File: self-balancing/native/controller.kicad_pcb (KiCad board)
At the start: 6 copper layers, 38 x 38 mm, 151 parts, among them J101 G, J102 5V, J103 T1, J104 R1, J105 G, J106 5V, J107 T2, J108 R2, J109 G, J110 5V, J111 T3, J112 R3, J113 G, J114 5V, J115 T4, J116 R4, J117 G, J118 3V3, J119 SCL, J120 SDA, J121 INT, J122 G, J123 G, J124 3V3, J125 SCK, J126 MISO, J127 MOSI, J128 CS, J129 G, J130 3V3, J131 CAN_RX, J132 CAN_TX, J133 G, J134 OUT1, J135 OUT2, J136 OUT3, J137 OUT4, J138 G, J139 OUT5, J140 OUT6, J141 OUT7, J142 OUT8, J143 G_LINK, J144 5V_LINK, J145 LINK_TX, J146 LINK_RX, J147 RUN, J148 M_OK, J149 G, J150 VTREF, J151 SWDIO, J152 SWCLK, J153 NRST, J154 BOOT, J155 G, J156 3V3, J157 ADC1, J158 ADC2, J159 ADC3, J160 RPM, J161 G, J162 3V3, J163 LED, J164 BUZ, J165 PC8, J166 PC9, J167 PD14, J2 TYPE-C-31-M-12, J3 MOTOR / 6-wire, J4 EXT SPI SENSOR, J5 GPS / UART4, Q1 2N7002, Q2 DMN2310UW-7, U1 STM32H743VIT6, U10 SN74LVC2G17DBVR, U11 W25N01GVZEIG / 128MiB, U12 TLV803EA29DBZR, U13 TPS2116DRLR, U2 TPS62162DSGR / 3.3V, U3 ICM-42688-P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

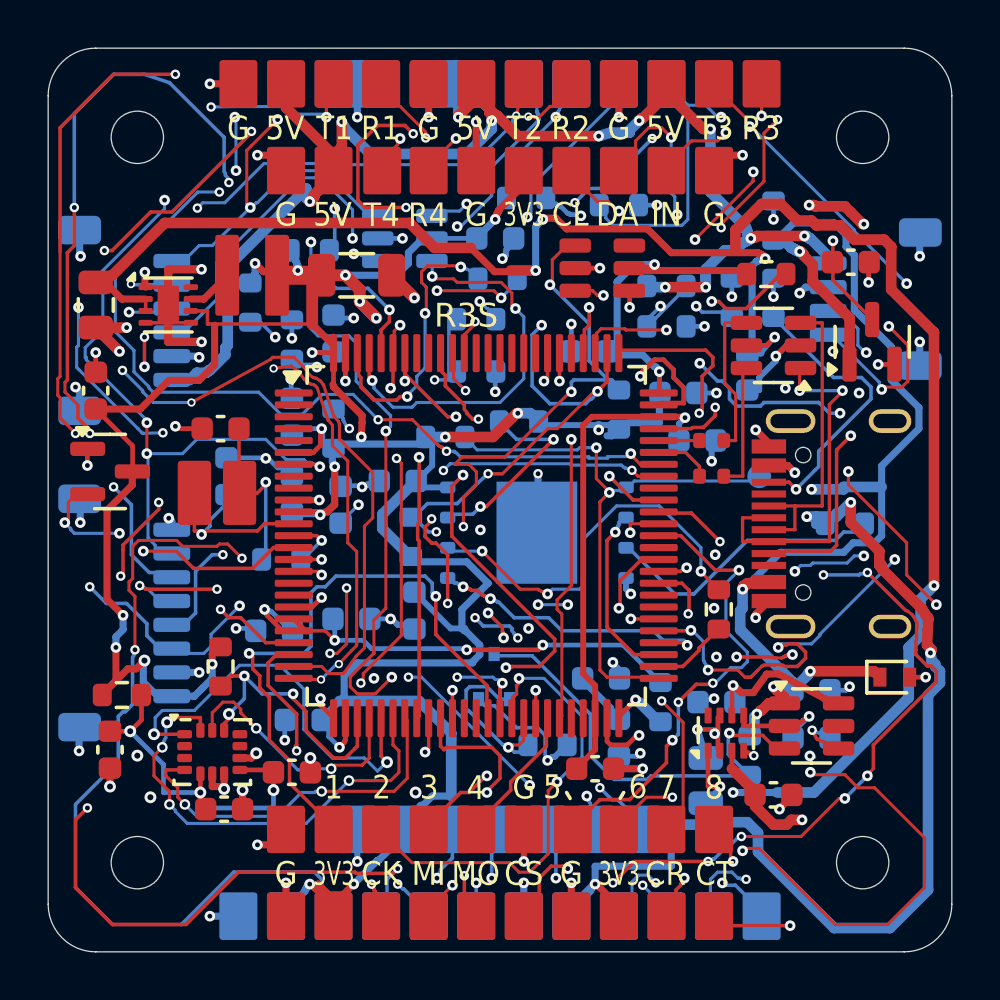
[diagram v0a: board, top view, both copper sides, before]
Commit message: Fix native USB routing and shallow via contacts
Native-only repair based on 491987e. Configured DRC/ERC/opens/parity pass. Keeps placement, BOM/CPL, 406 vias and 97 GND stitches. Manufacturing exports have not been regenerated; full validation evidence follows in this branch.
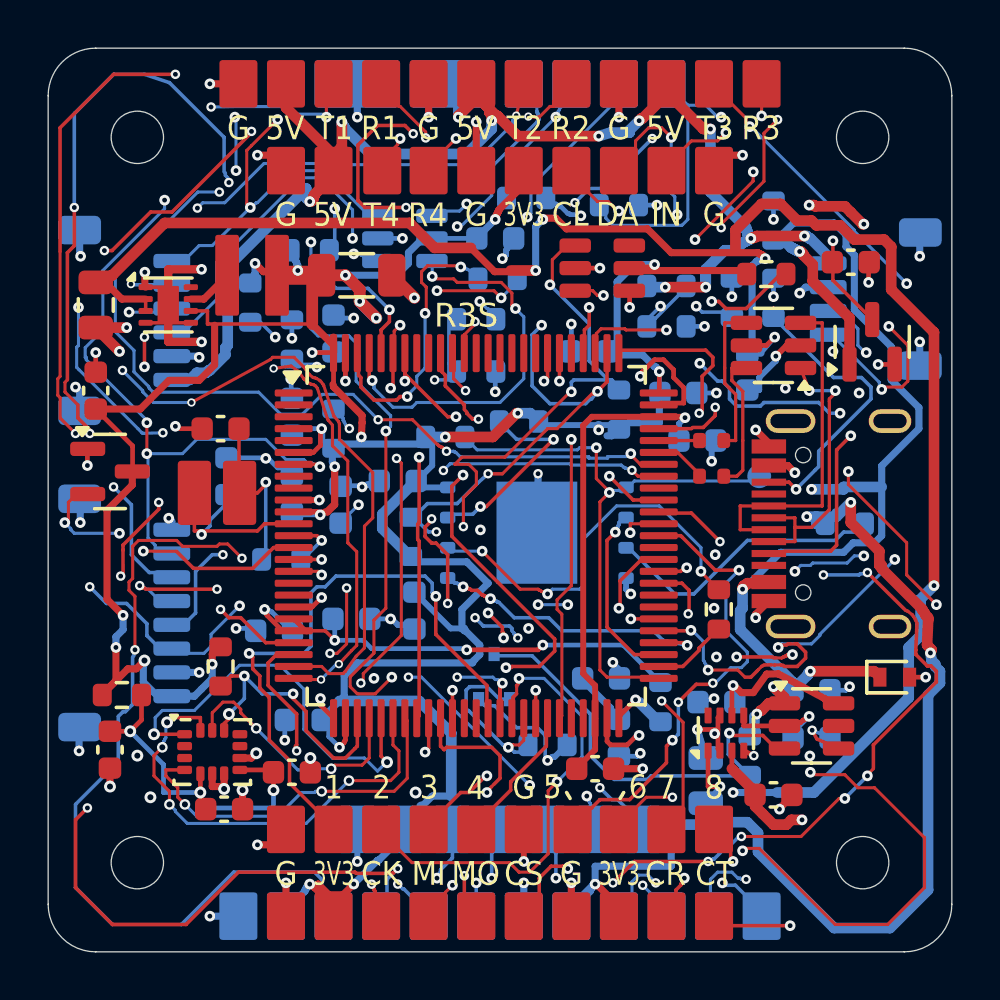
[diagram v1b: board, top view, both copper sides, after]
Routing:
- net /power/USB_CONN_N: track 15.1 -> 12.2 mm
- net /power/USB_CONN_P: track 13.0 -> 14.3 mm
- net /power/USB_ESD_N: track 5.50 -> 6.01 mm
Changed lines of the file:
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@@
 	)
 	(segment
-		(start 32.065878 29.8)
-		(end 32.029385 29.763507)
-		(width 0.2)
-		(layer "B.Cu")
-		(net "GND")
-	)
-	(segment
 		(start 36.675 13.35)
 		(end 36.65 13.35)
@@
 	)
 	(segment
-		(start 32.2 29.8)
-		(end 32.065878 29.8)
-		(width 0.2)
-		(layer "B.Cu")
-		(net "GND")
-	)
-	(segment
 		(start 10.25 18)
 		(end 9.9 17.65)
@@
 	)
 	(segment
-		(start 29.2092 18)
+		(start 28.7492 13.45)
+		(end 28.7492 13.976068)
+		(width 0.1392)
+		(layer "F.Cu")
+		(net "/power/USB_ESD_N")
+	)
+	(segment
+		(start 28.96 18)
 		(end 28.41 18)
 		(width 0.1392)
@@
 	)
 	(segment
-		(start 29.2092 13.45)
-		(end 29.2092 18)
+		(start 29.2092 17.7508)
+		(end 28.96 18)
+		(width 0.1392)
+		(layer "F.Cu")
+		(net "/power/USB_ESD_N")
+	)
+	(segment
+		(start 28.7492 13.976068)
+		(end 29.2092 14.436068)
 		(width 0.1392)
 		(layer "F.Cu")
@@
 	(segment
 		(start 29.3625 13.45)
-		(end 29.2092 13.45)
+		(end 28.7492 13.45)
+		(width 0.1392)
+		(layer "F.Cu")
+		(net "/power/USB_ESD_N")
+	)
+	(segment
+		(start 29.2092 16.5)
+		(end 29.2092 17.7508)
+		(width 0.1392)
+		(layer "F.Cu")
+		(net "/power/USB_ESD_N")
+	)
+	(segment
+		(start 29.2092 14.436068)
+		(end 29.2092 16.5)
 		(width 0.1392)
 		(layer "F.Cu")
@@
 	(segment
 		(start 27.39 18)
-		(end 27.39 17.59)
+		(end 27.39 17.92)
 		(width 0.1392)
 		(layer "F.Cu")
@@
 	)
 	(segment
-		(start 27.39 17.59)
-		(end 26.8 17)
+		(start 27.39 17.92)
+		(end 26.47 17)
 		(width 0.1392)
 		(layer "F.Cu")
@@
 	)
 	(segment
-		(start 26.8 17)
+		(start 26.47 17)
 		(end 25.675 17)
 		(width 0.1392)
@@
 	)
 	(segment
-		(start 22.95 14.65)
+		(start 23.1 14.43)
 		(end 22.85 14.75)
 		(width 0.15)
@@
 	)
 	(segment
-		(start 29.2 19.75)
-		(end 29.2 20.75)
+		(start 31.4 20.15)
+		(end 32.1 20.15)
 		(width 0.1392)
 		(layer "F.Cu")
@@
 	)
 	(segment
-		(start 31.6 13.4875)
+		(start 32 14.4)
 		(end 31.6375 13.45)
 		(width 0.1392)
@@
 	)
 	(segment
-		(start 29.2 20.75)
-		(end 30.305 20.75)
+		(start 32.1 20.15)
+		(end 32.8492 19.4008)
+		(width 0.1392)
+		(layer "F.Cu")
+		(net "/power/USB_CONN_N")
+	)
+	(segment
+		(start 31.4 20.75)
+		(end 31.4 19.75)
 		(width 0.1392)
 		(layer "F.Cu")
@@
 	)
 	(segment
-		(start 33.4 14.4357)
-		(end 33.4 14.4)
+		(start 31.4 19.75)
+		(end 30.305 19.75)
 		(width 0.1392)
 		(layer "F.Cu")
@@
 	)
 	(segment
-		(start 31.6 14.4)
-		(end 31.6 13.4875)
+		(start 33.1 14.5)
+		(end 33.1 14.4)
 		(width 0.1392)
 		(layer "F.Cu")
@@
 	)
 	(segment
-		(start 32.849199 20.75)
-		(end 32.849199 14.986501)
+		(start 32.8492 19.4008)
+		(end 32.8492 19.25)
 		(width 0.1392)
 		(layer "F.Cu")
@@
 	)
 	(segment
-		(start 30.305 19.75)
-		(end 29.2 19.75)
+		(start 32.8492 14.85)
+		(end 32.8492 14.7508)
 		(width 0.1392)
 		(layer "F.Cu")
@@
 	(segment
 		(start 30.305 20.75)
-		(end 32.849199 20.75)
+		(end 31.4 20.75)
+		(width 0.1392)
+		(layer "F.Cu")
+		(net "/power/USB_CONN_N")
+	)
+	(segment
+		(start 32.8492 19.25)
+		(end 32.8492 14.85)
 		(width 0.1392)
 		(layer "F.Cu")
@@
 	)
 	(segment
-		(start 32.849199 14.986501)
-		(end 33.4 14.4357)
+		(start 32.8492 14.7508)
+		(end 33.1 14.5)
 		(width 0.1392)
 		(layer "F.Cu")
@@
 	)
 	(via
-		(at 31.6 14.4)
+		(at 32 14.4)
 		(size 0.45)
 		(drill 0.2)
 		(layers "F.Cu" "B.Cu")
-		(capping no)
-		(covering
-			(front no)
-			(back no)
-		)
-		(plugging
-			(front no)
-			(back no)
-		)
-		(filling no)
 		(net "/power/USB_CONN_N")
 	)
 	(via
-		(at 33.4 14.4)
+		(at 33.1 14.4)
 		(size 0.45)
 		(drill 0.2)
 		(layers "F.Cu" "B.Cu")
-		(capping no)
-		(covering
-			(front no)
-			(back no)
-		)
-		(plugging
-			(front no)
-			(back no)
-		)
-		(filling no)
 		(net "/power/USB_CONN_N")
 	)
 	(segment
-		(start 33.4 14.4)
-		(end 31.6 14.4)
+		(start 33.1 14.4)
+		(end 32 14.4)
 		(width 0.1392)
 		(layer "B.Cu")
@@
 	)
 	(segment
-		(start 32.549999 11.55)
-		(end 31.6375 11.55)
+		(start 29.1 19.25)
+		(end 29.1 20.25)
 		(width 0.1392)
 		(layer "F.Cu")
@@
 	)
 	(segment
-		(start 31.4 20.25)
+		(start 30.305 19.25)
+		(end 32.549999 19.25)
+		(width 0.1392)
+		(layer "F.Cu")
+		(net "/power/USB_CONN_P")
+	)
+	(segment
+		(start 29.1 20.25)
 		(end 30.305 20.25)
 		(width 0.1392)
@@
 	)
 	(segment
-		(start 32.549999 19.25)
-		(end 32.549999 11.55)
+		(start 30.305 19.25)
+		(end 29.1 19.25)
 		(width 0.1392)
 		(layer "F.Cu")
@@
 	)
 	(segment
-		(start 31.4 19.25)
-		(end 31.4 20.25)
+		(start 32.549999 11.55)
+		(end 31.6375 11.55)
 		(width 0.1392)
 		(layer "F.Cu")
@@
 	)
 	(segment
-		(start 30.305 19.25)
-		(end 32.549999 19.25)
+		(start 32.549999 14.85)
+		(end 32.549999 11.55)
+		(width 0.1392)
+		(layer "F.Cu")
+		(net "/power/USB_CONN_P")
+	)
+	(segment
+		(start 32.549999 19.25)
+		(end 32.549999 14.85)
 		(width 0.1392)
 		(layer "F.Cu")
@@
 	(segment
 		(start 28.45 11.55)
-		(end 28.45 14.1)
+		(end 28.45 13.45)
 		(width 0.1392)
 		(layer "F.Cu")
@@
 	)
 	(segment
+		(start 28.45 13.45)
+		(end 28.45 14.1)
+		(width 0.1392)
+		(layer "F.Cu")
+		(net "/power/USB_ESD_P")
+	)
+	(segment
 		(start 28.91 16.5)
 		(end 28.41 16.5)
@@
 	)
 	(segment
-		(start 26.75 24.9)
+		(start 26.872965 25.109661)
 		(end 25.85 24.9)
 		(width 0.15)
